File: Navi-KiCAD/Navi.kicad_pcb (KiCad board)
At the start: 4 copper layers, 50.8 x 40 mm, 216 parts, among them J1 0734120110, J2 0734120110, J3 0734120110, J4 473460001, J5 AXK5S80047YG, J6 AXK5S80047YG, Q1 IRLML5203TRPBF, Q2 IRLML5203TRPBF, U1 LP55231SQE/NOPB, U10 TPS54232DR, U11 MPU-9250, U12 LPS25HBTR, U13 NUF2042XV6T1G, U14 LTC4412ES6#TRPBF, U15 MIC94082YFT-TR, U16 LSM6DS33, U17 LSM303AH, U2 Logo, U3 Logo, U4 ATSAME70Q21A-AN, U5 CC1310F128RGZR, U6 CC1190RGVR, U7 CC2650F128RGZR, U8 CC2592RGVR, U9 MAX-M8W-0, Y1 9HT11-32.768KDZB-T, Y2 7V-16.000MAHJ-T, Y3 XRCGB24M000F2P00R0, Y4 XRCGB24M000F2P00R0

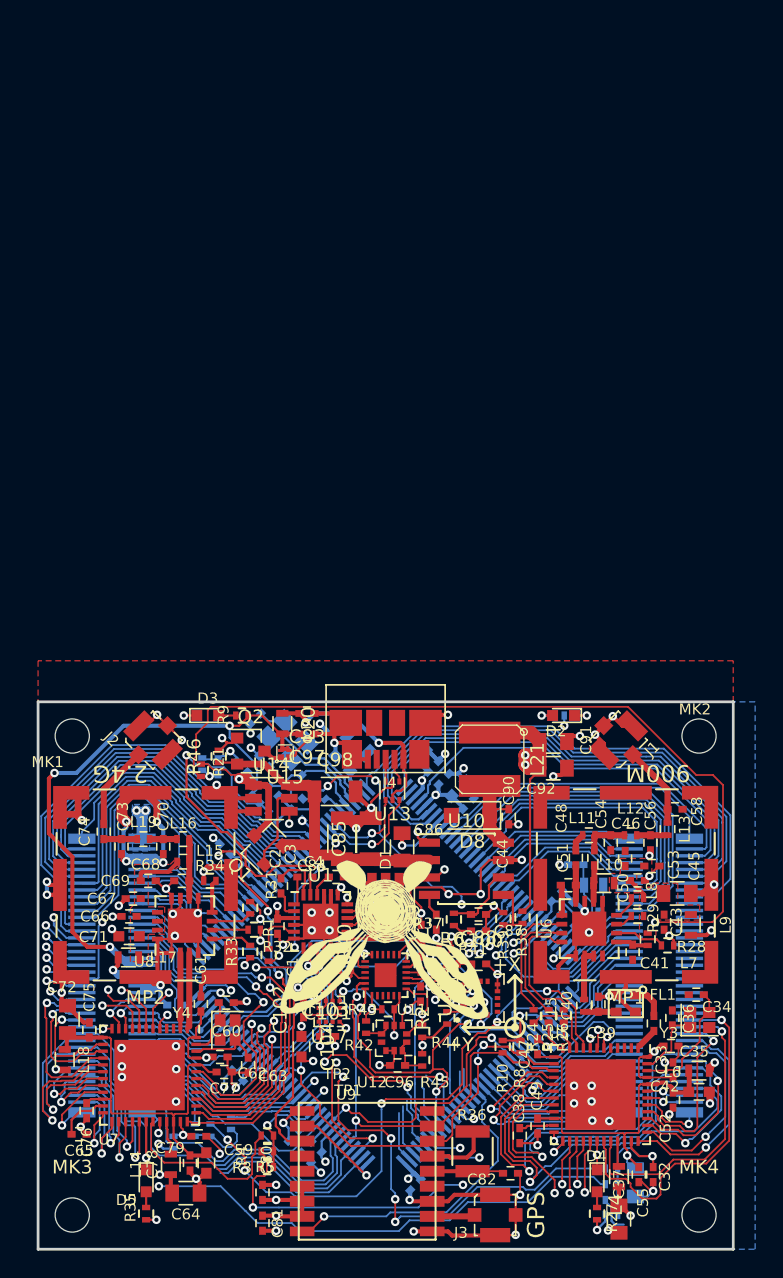
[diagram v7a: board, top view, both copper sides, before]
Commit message: Finished reroute
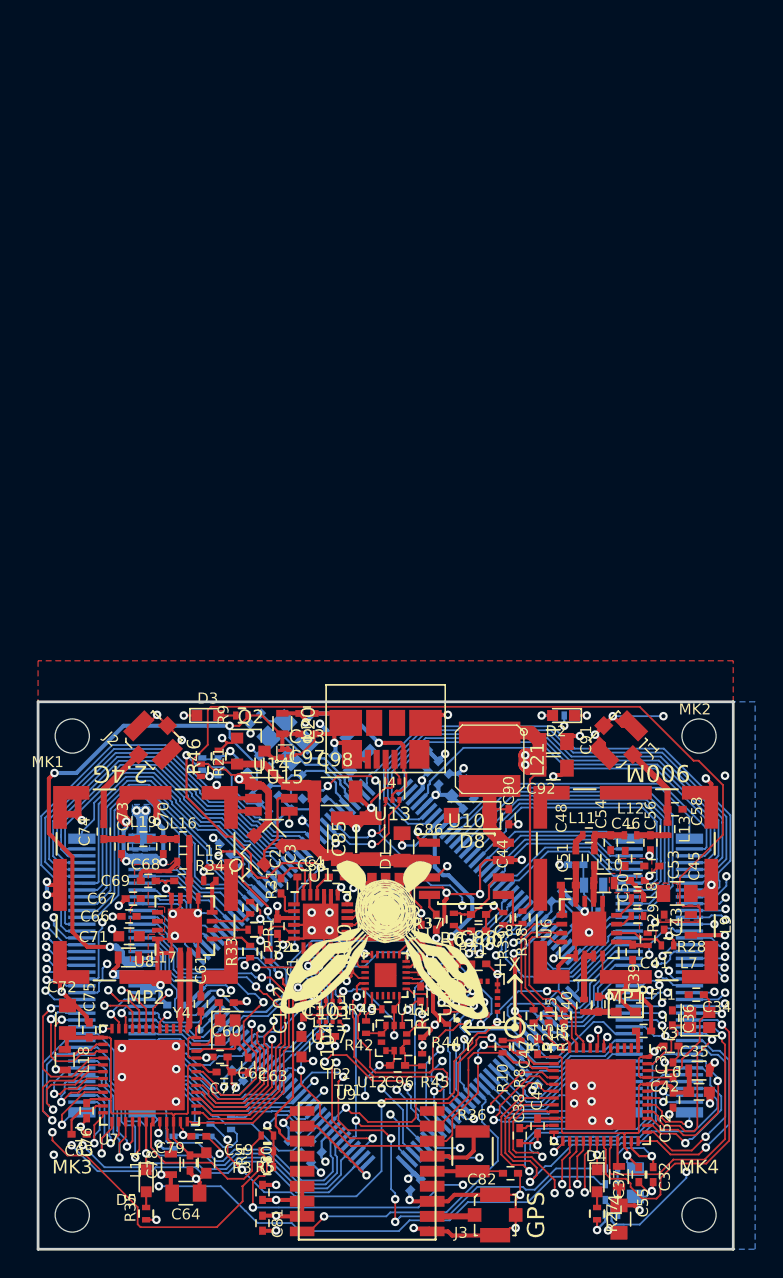
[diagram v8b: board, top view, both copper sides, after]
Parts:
- moved C39 0.93 mm to (93.8, 109.0), turned to 0 degrees
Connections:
- J5 pad 30: Net-(J5-Pad30) -> /LED_D1
- J5 pad 32: Net-(J5-Pad32) -> /LED_D2
- J5 pad 34: Net-(J5-Pad34) -> /Connectors/2.4-ADIO-29
- J5 pad 36: Net-(J5-Pad36) -> /Connectors/2.4-ADIO-28
- J5 pad 38: Net-(J5-Pad38) -> /Connectors/2.4-ADIO-27
- J5 pad 40: Net-(J5-Pad40) -> /Connectors/2.4-ADIO-26
- J5 pad 42: Net-(J5-Pad42) -> /CPU_RESET_EXT
- J5 pad 44: Net-(J5-Pad44) -> /Connectors/PC28
- J5 pad 46: Net-(J5-Pad46) -> /LED_D9R
- J5 pad 48: Net-(J5-Pad48) -> /Connectors/PD17
- J6 pad 17: Net-(J6-Pad17) -> /Power-~SHDN~
- J6 pad 19: Net-(J6-Pad19) -> /LED_D3
- J6 pad 21: Net-(J6-Pad21) -> /LED_D4
- J6 pad 23: Net-(J6-Pad23) -> /LED_D8R
- J6 pad 25: Net-(J6-Pad25) -> /Connectors/AUX_SCL
- J6 pad 27: Net-(J6-Pad27) -> /Connectors/PA18
- J6 pad 29: Net-(J6-Pad29) -> /Connectors/AUX_SDA
- J6 pad 31: Net-(J6-Pad31) -> /Connectors/PA17
- J6 pad 33: Net-(J6-Pad33) -> /Connectors/PA19
- J6 pad 35: Net-(J6-Pad35) -> /Connectors/PE4
- J6 pad 37: Net-(J6-Pad37) -> /Connectors/PB2
- J6 pad 39: Net-(J6-Pad39) -> /Connectors/900-DIO-18
- J6 pad 41: Net-(J6-Pad41) -> /Connectors/900-DIO-19
- J6 pad 43: Net-(J6-Pad43) -> /Connectors/900-DIO-20
- J6 pad 44: Net-(J6-Pad44) -> /Connectors/PC5
- J6 pad 45: Net-(J6-Pad45) -> /Connectors/900-DIO-17
- J6 pad 46: Net-(J6-Pad46) -> /Connectors/PA25
- J6 pad 47: Net-(J6-Pad47) -> /Connectors/900-DIO-16
- J6 pad 48: Net-(J6-Pad48) -> /Connectors/PA11
- J6 pad 49: Net-(J6-Pad49) -> /Connectors/900-DIO-14
- J6 pad 50: Net-(J6-Pad50) -> /Connectors/PA26
- J6 pad 51: Net-(J6-Pad51) -> /900_RESET_EXT
- J6 pad 52: Net-(J6-Pad52) -> /Connectors/PA12
- J6 pad 54: Net-(J6-Pad54) -> /Connectors/PA27
- J6 pad 56: Net-(J6-Pad56) -> /Connectors/PD28
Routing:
- net +3V3: track 102.9 -> 334.4 mm, vias 29 -> 32
- net /CPU_RESET_EXT: track 0.00 -> 51.4 mm, vias 0 -> 3
- net /Connectors/AUX_SDA: track 9.71 -> 48.0 mm, vias 2 -> 3
- net /LED_D8R: track 0.70 -> 37.5 mm, vias 1 -> 4
- net /Connectors/AUX_SCL: track 12.1 -> 46.6 mm, vias 2 -> 3
- net /Connectors/900-DIO-16: track 3.38 -> 34.8 mm, vias 1 -> 2
- net /Connectors/900-DIO-14: track 11.2 -> 42.4 mm, vias 1 -> 2
- net /LED_D3: track 2.06 -> 32.6 mm, vias 1 -> 2
- net /Connectors/900-DIO-18: track 3.33 -> 33.6 mm, vias 1 -> 2
- net /LED_D4: track 2.97 -> 32.9 mm, vias 1 -> 2
- net /Connectors/900-DIO-20: track 2.10 -> 30.9 mm, vias 1 -> 2
- net /LED_D2: track 0.50 -> 28.9 mm, vias 1 -> 2
- net /Connectors/PA27: track 3.84 -> 32.2 mm, vias 0 -> 2
- net /Connectors/900-DIO-17: track 4.01 -> 32.2 mm, vias 1 -> 2
- net /Connectors/PC28: track 12.9 -> 40.3 mm, vias 0 -> 2
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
